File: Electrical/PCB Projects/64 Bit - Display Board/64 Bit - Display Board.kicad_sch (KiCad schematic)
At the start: 0 parts

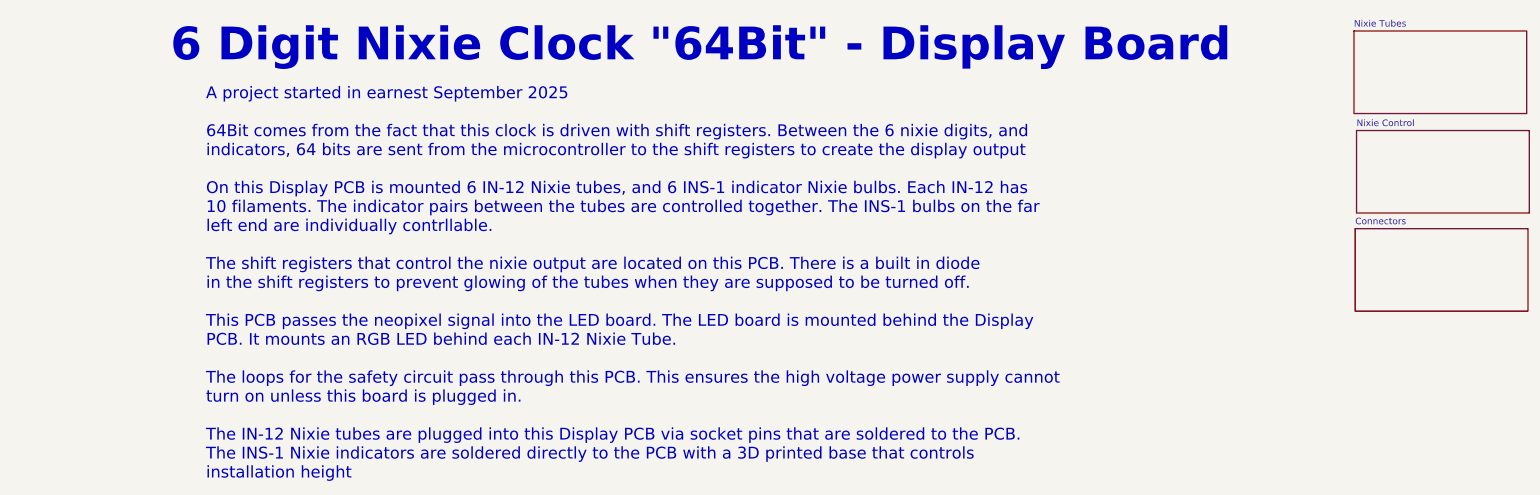
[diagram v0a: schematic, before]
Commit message: near final state. Includes BOM, price, etc
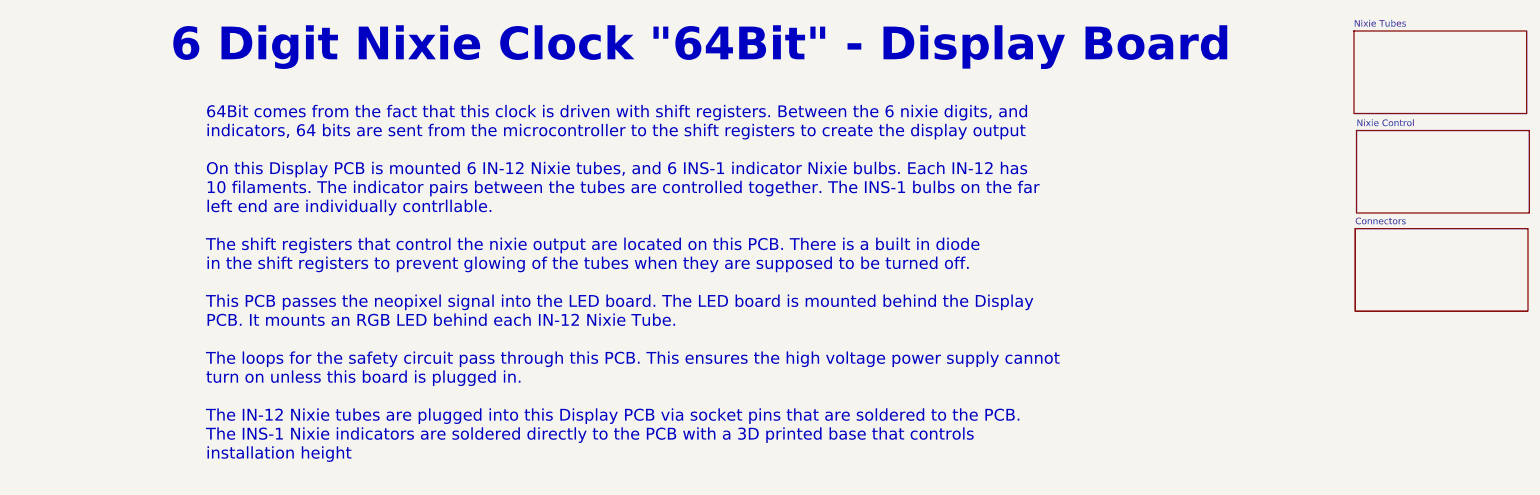
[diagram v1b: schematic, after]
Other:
- note added: "64Bit comes from the fact that this clock is driven with shift registers. Between the 6 nixie digits, and indicators, 64 bits are sent from the microcontroller to the shift registers to create the display output On this Display PCB is mounted 6 IN-12 Nixie tubes, and 6 INS-1 indicator Nixie bulbs. Each IN-12 has 10 filaments. The indicator pairs between the tubes are controlled together. The INS-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"
- note removed: "A project started in earnest September 2025 64Bit comes from the fact that this clock is driven with shift registers. Between the 6 nixie digits, and indicators, 64 bits are sent from the microcontroller to the shift registers to create the display output On this Display PCB is mounted 6 IN-12 Nixie tubes, and 6 INS-1 indicator Nixie bulbs. Each IN-12 has 10 filaments. The indicator pairs between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"
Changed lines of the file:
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@@
 	(title_block
 		(title "Project Overview")
-		(date "2025-10-04")
+		(date "2025-12-01")
 		(rev "1")
 		(company "Kadin Whiting")
@@
 		)
 	)
-	(text "A project started in earnest September 2025\n\n64Bit comes from the fact that this clock is driven with shift registers. Between the 6 nixie digits, and \nindicators, 64 bits are sent from the microcontroller to the shift registers to create the display output\n\nOn this Display PCB is mounted 6 IN-12 Nixie tubes, and 6 INS-1 indicator Nixie bulbs. Each IN-12 has\n10 filaments. The indicator pairs between the tubes are controlled together. The INS-1 bulbs on the far\nleft end are individually contrllable.\n\nThe shift registers that control the nixie output are located on this PCB. There is a built in diode\nin the shift registers to prevent glowing of the tubes when they are supposed to be turned off.\n\nThis PCB passes the neopixel signal into the LED board. The LED board is mounted behind the Display\nPCB. It mounts an RGB LED behind each IN-12 Nixie Tube.\n\nThe loops for the safety circuit pass through this PCB. This ensures the high voltage power supply cannot\nturn on unless this board is plugged in.\n\nThe IN-12 Nixie tubes are plugged into this Display PCB via socket pins that are soldered to the PCB.\nThe INS-1 Nixie indicators are soldered directly to the PCB with a 3D printed base that controls \ninstallation height"
+	(text "64Bit comes from the fact that this clock is driven with shift registers. Between the 6 nixie digits, and \nindicators, 64 bits are sent from the microcontroller to the shift registers to create the display output\n\nOn this Display PCB is mounted 6 IN-12 Nixie tubes, and 6 INS-1 indicator Nixie bulbs. Each IN-12 has\n10 filaments. The indicator pairs between the tubes are controlled together. The INS-1 bulbs on the far\nleft end are individually contrllable.\n\nThe shift registers that control the nixie output are located on this PCB. There is a built in diode\nin the shift registers to prevent glowing of the tubes when they are supposed to be turned off.\n\nThis PCB passes the neopixel signal into the LED board. The LED board is mounted behind the Display\nPCB. It mounts an RGB LED behind each IN-12 Nixie Tube.\n\nThe loops for the safety circuit pass through this PCB. This ensures the high voltage power supply cannot\nturn on unless this board is plugged in.\n\nThe IN-12 Nixie tubes are plugged into this Display PCB via socket pins that are soldered to the PCB.\nThe INS-1 Nixie indicators are soldered directly to the PCB with a 3D printed base that controls \ninstallation height"
 		(exclude_from_sim no)
 		(at 23.368 68.58 0)

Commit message: slight changes
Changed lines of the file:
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@@
 		)
 	)
-	(text "64Bit comes from the fact that this clock is driven with shift registers. Between the 6 nixie digits, and \nindicators, 64 bits are sent from the microcontroller to the shift registers to create the display output\n\nOn this Display PCB is mounted 6 IN-12 Nixie tubes, and 6 INS-1 indicator Nixie bulbs. Each IN-12 has\n10 filaments. The indicator pairs between the tubes are controlled together. The INS-1 bulbs on the far\nleft end are individually contrllable.\n\nThe shift registers that control the nixie output are located on this PCB. There is a built in diode\nin the shift registers to prevent glowing of the tubes when they are supposed to be turned off.\n\nThis PCB passes the neopixel signal into the LED board. The LED board is mounted behind the Display\nPCB. It mounts an RGB LED behind each IN-12 Nixie Tube.\n\nThe loops for the safety circuit pass through this PCB. This ensures the high voltage power supply cannot\nturn on unless this board is plugged in.\n\nThe IN-12 Nixie tubes are plugged into this Display PCB via socket pins that are soldered to the PCB.\nThe INS-1 Nixie indicators are soldered directly to the PCB with a 3D printed base that controls \ninstallation height"
+	(text "64Bit comes from the fact that this clock is driven with shift registers. Between the 6 nixie digits, and \nindicators, 64 bits are sent from the microcontroller to the shift registers to create the display output\n\nOn this Display PCB is mounted 6 IN-12 Nixie tubes, and 6 INS-1 indicator Nixie bulbs. Each IN-12 has\n10 filaments. The indicator pairs between the tubes are controlled together. The INS-1 bulbs on the far\nleft end are individually controllable.\n\nThe shift registers that control the nixie output are located on this PCB. There is a built in diode\nin the shift registers to prevent glowing of the tubes when they are supposed to be turned off.\n\nThis PCB passes the neopixel signal into the LED board. The LED board is mounted behind the Display\nPCB. It mounts an RGB LED behind each IN-12 Nixie Tube.\n\nThe loops for the safety circuit pass through this PCB. This ensures the high voltage power supply cannot\nturn on unless this board is plugged in.\n\nThe IN-12 Nixie tubes are plugged into this Display PCB via socket pins that are soldered to the PCB.\nThe INS-1 Nixie indicators are soldered directly to the PCB with a 3D printed base that controls \ninstallation height"
 		(exclude_from_sim no)
 		(at 23.368 68.58 0)
